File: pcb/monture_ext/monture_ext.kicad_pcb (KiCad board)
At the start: 2 copper layers, 150 x 110 mm, 37 parts, among them U1 Teensy 4.1

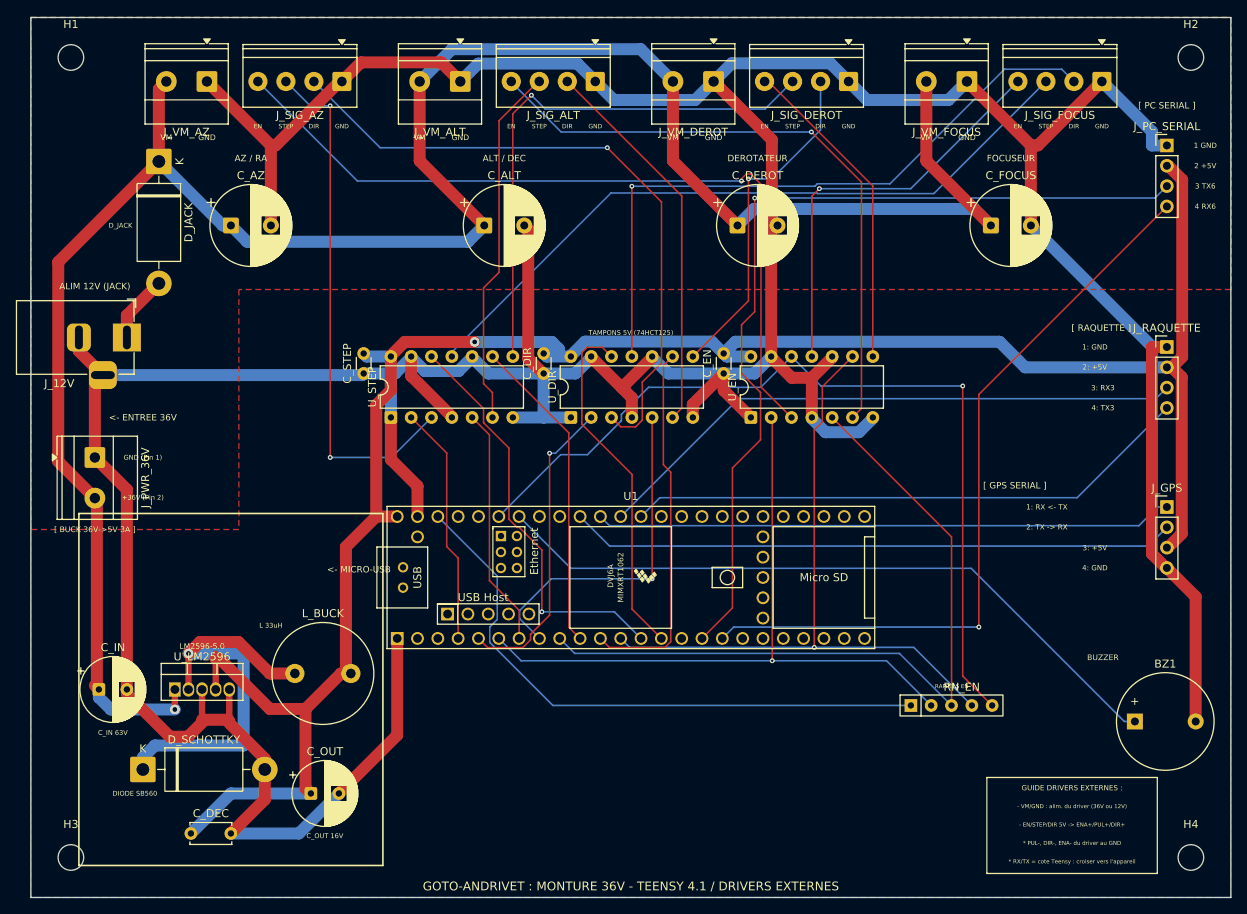
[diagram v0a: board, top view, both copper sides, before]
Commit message: Cartes : sérigraphie lisible, LM2596HV, 74ACT125, fichiers de fabrication
Sérigraphie des trois cartes refaite : tous les textes à 1 mm de haut et
0,15 mm de trait (règle DRC des .kicad_pro relevée à ces valeurs), plus
aucun texte sur un autre, sur une pastille ou hors de la carte.
- références des borniers dans leur bande libre, repères 1B/1A/2A/2B
  centrés sous les vis ;
- broches des connecteurs PC, raquette, GPS, LCD et Grove numérotées en
  face de chaque broche, côté Teensy (RX4/TX4, RX3/TX3, TX6/RX6) ;
- guides de câblage réécrits pour tenir en 1 mm ;
- cadre du buck retiré (il passait sur le trou H3 et le bornier 36V),
  références des trous de fixation masquées, marquages de la puce du
  Teensy passés sur la couche de fabrication ;
- raquette : titre centré (il sortait de la carte), repères sous chaque
  fil du câble vers la monture.
Cuivre, zones et pastilles inchangés (vérifiés identiques). DRC : 0
erreur, 0 non connecté ; seul reste l'avertissement du jack 12 V, qui
dépasse volontairement du bord.

Buck : LM2596HVT-5.0 (60 V en entrée) au lieu du LM2596-5.0 limité à
40 V sur un bus 36 V. Même boîtier, même brochage, même fréquence.

Carte drivers externes : 74ACT125 au lieu du 74HCT125. Entrées TTL
identiques, mais 24 mA par sortie au lieu de 6, pour les optocoupleurs
des drivers qui tirent 7 à 16 mA.

build_kicad_pcbs.py porte la nouvelle sérigraphie : il reproduit les
cartes routées. Nouveau fabrication.py : Gerber et perçages, liste des
composants regroupée par pièce à acheter, vues 3D, dans pcb/fabrication/.

Co-Authored-By: Claude Opus 5.5 <noreply@anthropic.com>
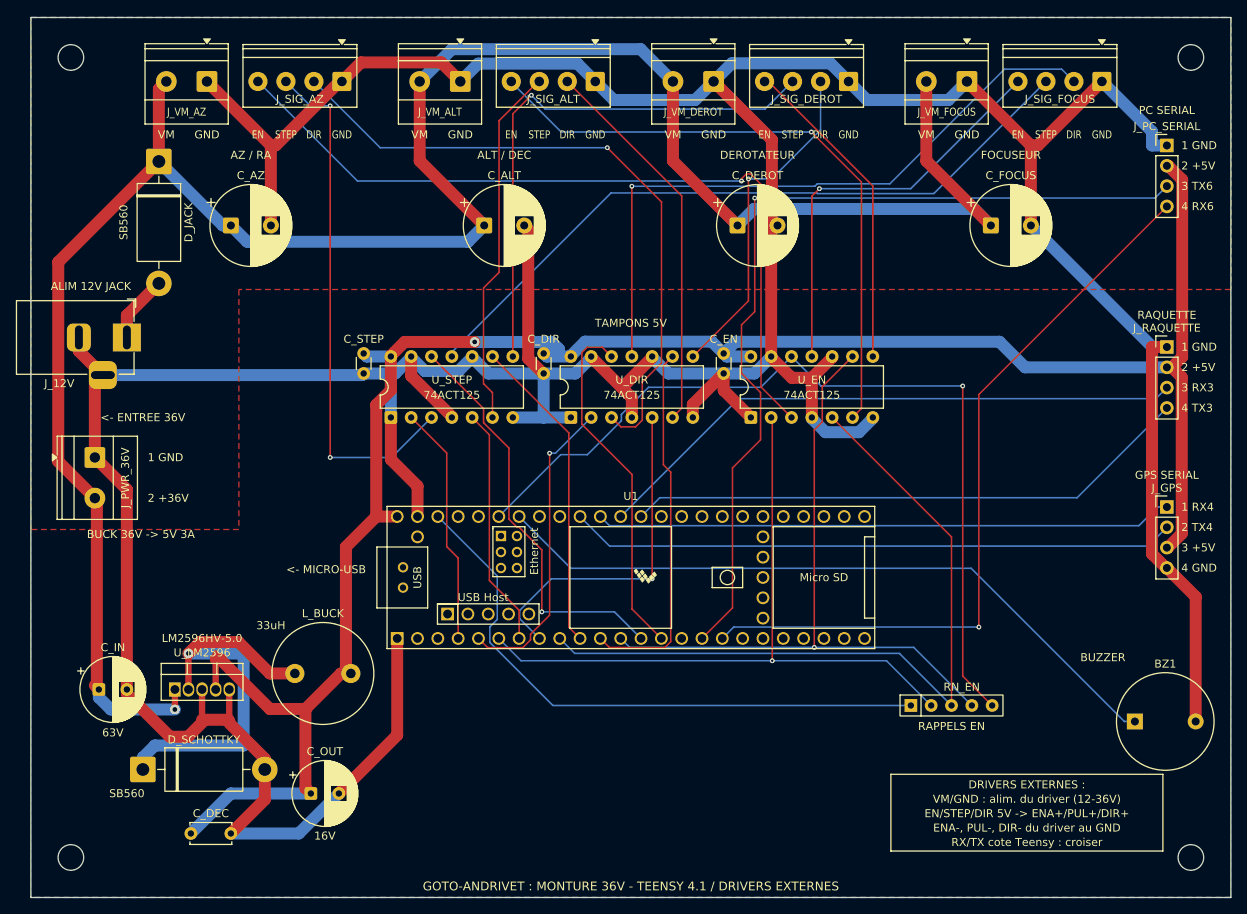
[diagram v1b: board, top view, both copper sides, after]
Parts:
- U_DIR, U_EN, U_STEP: value 74HCT125 -> 74ACT125
- U_LM2596: value LM2596-5.0 -> LM2596HVT-5.0
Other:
- board text added: "1 RX4"
- board text added: "16V"
- board text added: "2 +36V"
- board text added: "2 TX4"
- board text added: "3 +5V"
- board text added: "3 RX3"
- board text added: "33uH"
- board text added: "4 GND"
- board text added: "4 TX3"
- board text added: "63V"
- board text added: "74ACT125"
- board text added: "ALIM 12V JACK"
- board text added: "BUCK 36V -> 5V 3A"
- board text added: "DRIVERS EXTERNES :"
- board text added: "EN/STEP/DIR 5V -> ENA+/PUL+/DIR+"
- board text added: "ENA-, PUL-, DIR- du driver au GND"
- board text added: "GPS SERIAL"
- board text added: "LM2596HV-5.0"
- board text added: "PC SERIAL"
- board text added: "RAQUETTE"
- board text added: "RX/TX cote Teensy : croiser"
- board text added: "SB560"
- board text added: "TAMPONS 5V"
- board text added: "VM/GND : alim. du driver (12-36V)"
- board text removed: "* PUL-, DIR-, ENA- du driver au GND"
- board text removed: "* RX/TX = cote Teensy : croiser vers l'appareil"
- board text removed: "+36V (Pin 2)"
- board text removed: "- EN/STEP/DIR 5V -> ENA+/PUL+/DIR+"
- board text removed: "- VM/GND : alim. du driver (36V ou 12V)"
- board text removed: "1: GND"
- board text removed: "1: RX <- TX"
- board text removed: "2: +5V"
- board text removed: "2: TX -> RX"
- board text removed: "3: +5V"
- board text removed: "3: RX3"
- board text removed: "4: GND"
- board text removed: "4: TX3"
- board text removed: "ALIM 12V (JACK)"
- board text removed: "C_IN 63V"
- board text removed: "C_OUT 16V"
- board text removed: "DIODE SB560"
- board text removed: "D_JACK"
- board text removed: "GND (Pin 1)"
- board text removed: "GUIDE DRIVERS EXTERNES :"
- board text removed: "L 33uH"
- board text removed: "LM2596-5.0"
- board text removed: "TAMPONS 5V (74HCT125)"
- board text removed: "[ BUCK 36V->5V 3A ]"
- board text removed: "[ GPS SERIAL ]"
- board text removed: "[ PC SERIAL ]"
- board text removed: "[ RAQUETTE ]"

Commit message: Cartes : protection de l'alimentation, buzzer sur transistor, I2C de la raquette en 3,3 V
Corrige les points trouvés à la vérification électrique (MCP KiCad).

Cartes monture (StepStick et drivers externes) :
- Entrée : D_JACK remplacée par D_IN, double diode Schottky MBR20100CT à
  cathode commune, une anode pour le bornier 36V et une pour le jack.
  Des fils inversés ou un jack à centre négatif ne passent plus ; puis
  F_IN, fusible TR5 temporisé 4 A sur support, commun aux deux entrées.
  Nouveaux réseaux PWR_IN et VIN_OR, en classe Puissance (1,5 mm).
- Buzzer : il était branché en direct sur la broche 20, alors qu'un
  buzzer passif tire 80 à 200 mA. Il est maintenant commandé par un
  PN2222A (1 kOhm sur la base, 10 kOhm de rappel au démarrage), alimenté
  en 5V à travers 68 Ohm, avec une diode 1N4148 à ses bornes.
- Sérigraphie « PC SERIAL 3V3 » : l'adaptateur USB-série doit être en
  3,3 V.

Carte raquette : adaptateur de niveau I2C à deux BSS138 (et quatre
10 kOhm). L'afficheur et la prise Grove restent en 5V ; le Teensy, qui
ne supporte pas le 5V, ne voit plus que du 3,3V sur SDA et SCL.

Routage refait par Freerouting (pistes du buck et amorces verrouillées
conservées, plans de cuivre de la carte externe remis). Deux broches OE
des 74ACT125, reliées au GND par piste, sont sorties du plan GND faute
de place pour leurs branches thermiques. DRC des trois cartes : 0
erreur, 0 non connecté ; le générateur reproduit exactement les cartes
routées. Assemblages FreeCAD mis à jour : aucune collision avec les
boîtiers ni avec les boutons.

Fichiers de fabrication, liste des composants, vues 3D, modèles .glb
et aperçus régénérés.

Co-Authored-By: Claude Opus 5.5 <noreply@anthropic.com>
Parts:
- removed D_JACK: SB560 (60V 5A), D_DO-201AD_P15.24mm_Horizontal
- added D_BUZ: 1N4148, D_DO-35_SOD27_P2.54mm_Vertical_AnodeUp, F.Cu at (124.0, 82.0)
- added D_IN: MBR20100CT, TO-220-3_Vertical, F.Cu at (12.0, 17.2)
- added F_IN: T4A (TR5), Fuse_Littelfuse_372_D8.50mm, F.Cu at (16.0, 27.3)
- added Q_BUZ: PN2222A, TO-92_Inline_Wide, F.Cu at (121.0, 77.0)
- added R_BUZ: 68, R_Axial_DIN0204_L3.6mm_D1.6mm_P2.54mm_Vertical, F.Cu at (128.0, 72.0)
- added R_BUZ_B: 1k, R_Axial_DIN0204_L3.6mm_D1.6mm_P2.54mm_Vertical, F.Cu at (116.0, 72.0)
- added R_BUZ_PD: 10k, R_Axial_DIN0204_L3.6mm_D1.6mm_P2.54mm_Vertical, F.Cu at (116.0, 82.0)
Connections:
- BZ1 pad 1: BUZZER -> BUZ_A
- BZ1 pad 2: GND -> BUZ_C
- J_PWR_36V pad 2: +36V -> PWR_IN
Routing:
- net GND: track 604.4 -> 657.0 mm, vias 0 -> 1
- net PWR_IN: track 0.00 -> 41.8 mm
- net BUZ_A: track 0.00 -> 29.8 mm
- net BUZZER: track 87.6 -> 59.0 mm
- net BUZ_C: track 0.00 -> 26.7 mm
- net BUZ_B: track 0.00 -> 18.1 mm
- net JACK_IN: track 8.42 -> 25.6 mm
- net AZ_STEP_EXT: track 65.5 -> 49.5 mm, vias 2 -> 0
- net FOCUS_DIR_EXT: track 83.2 -> 69.5 mm, vias 1 -> 0
- net +36V: track 275.8 -> 289.0 mm, vias 1 -> 4
- net DEROT_EN: track 85.7 -> 97.2 mm, vias 1 -> 0
- net AZ_DIR_EXT: track 82.6 -> 71.5 mm
- net VIN_OR: track 0.00 -> 10.4 mm
- net +5V: track 262.5 -> 272.8 mm, vias 1 -> 0
- net PC_TX: track 95.0 -> 104.7 mm
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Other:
- board text added: "MBR20100CT"
- board text added: "PC SERIAL 3V3"
- board text added: "T4A"
- board text removed: "PC SERIAL"
